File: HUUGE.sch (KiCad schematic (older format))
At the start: 21 parts, among them IC701 ADS122C04IPWR, U701 MAX5217GUA+, U702 MAX5217GUA+

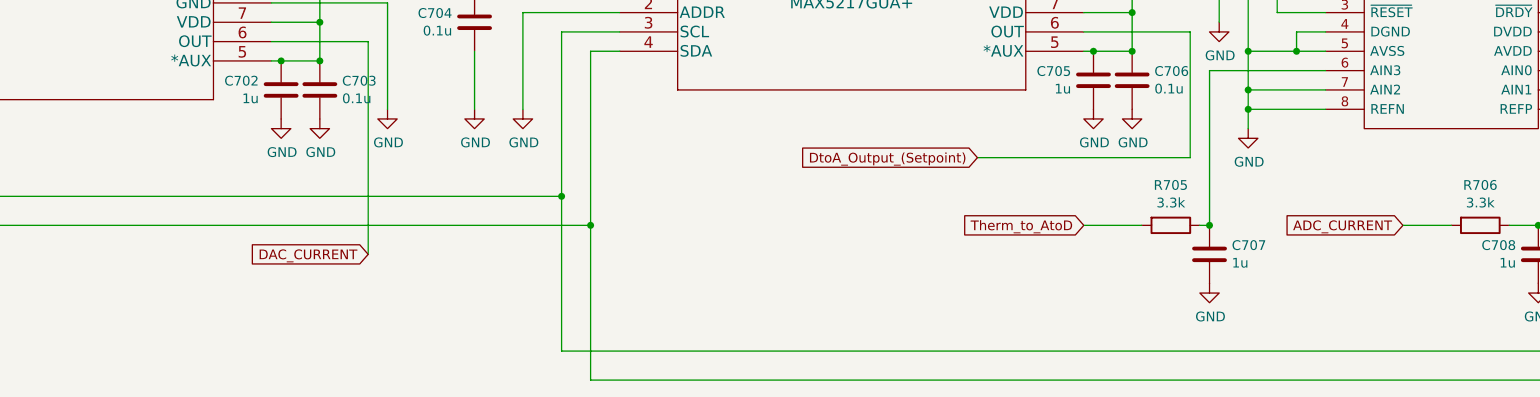
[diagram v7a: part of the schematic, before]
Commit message: adding labels
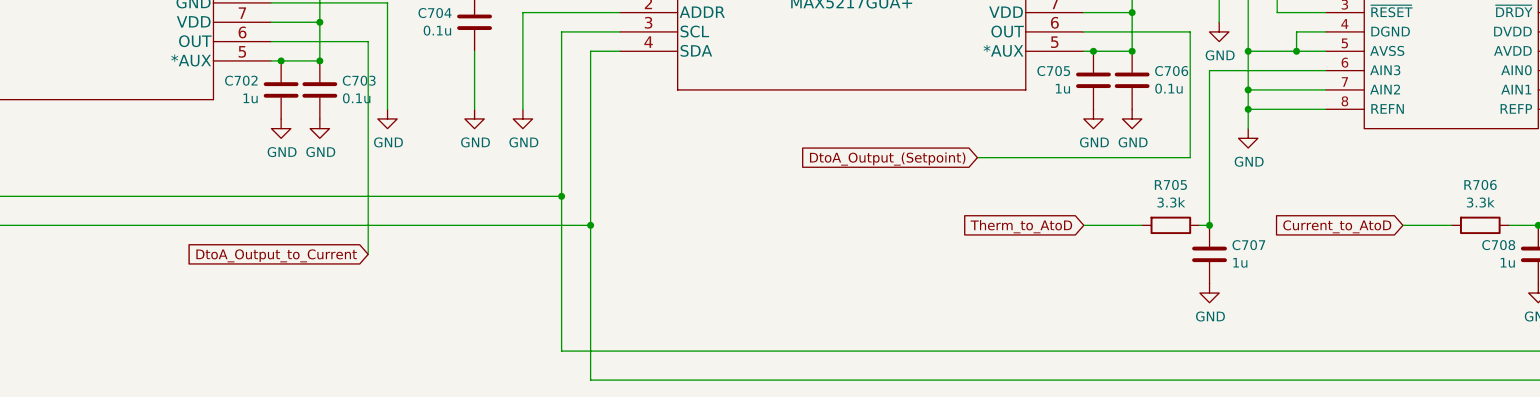
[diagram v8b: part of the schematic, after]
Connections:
- net ADC_CURRENT renamed Current_to_AtoD
- net DAC_CURRENT renamed DtoA_Output_to_Current
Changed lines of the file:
@@
 	12500 5500 12250 5500
 Text GLabel 12250 5500 0    50   Input ~ 0
-ADC_CURRENT
+Current_to_AtoD
 $Comp
 L power:GND #PWR0714
@@
 	6900 4550 6900 5650
 Text GLabel 6900 5650 0    50   Input ~ 0
-DAC_CURRENT
+DtoA_Output_to_Current
 Wire Wire Line
 	13150 4900 13150 5500
